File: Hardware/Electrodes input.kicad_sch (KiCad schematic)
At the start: 36 parts, among them J2 Conn_01x26_Pin, U10 TPD4E1B06DCKR, U2 TPD4E1B06DCKR, U3 TPD4E1B06DCKR, U4 TPD4E1B06DCKR, U5 TPD4E1B06DCKR, U9 TPD4E1B06DCKR

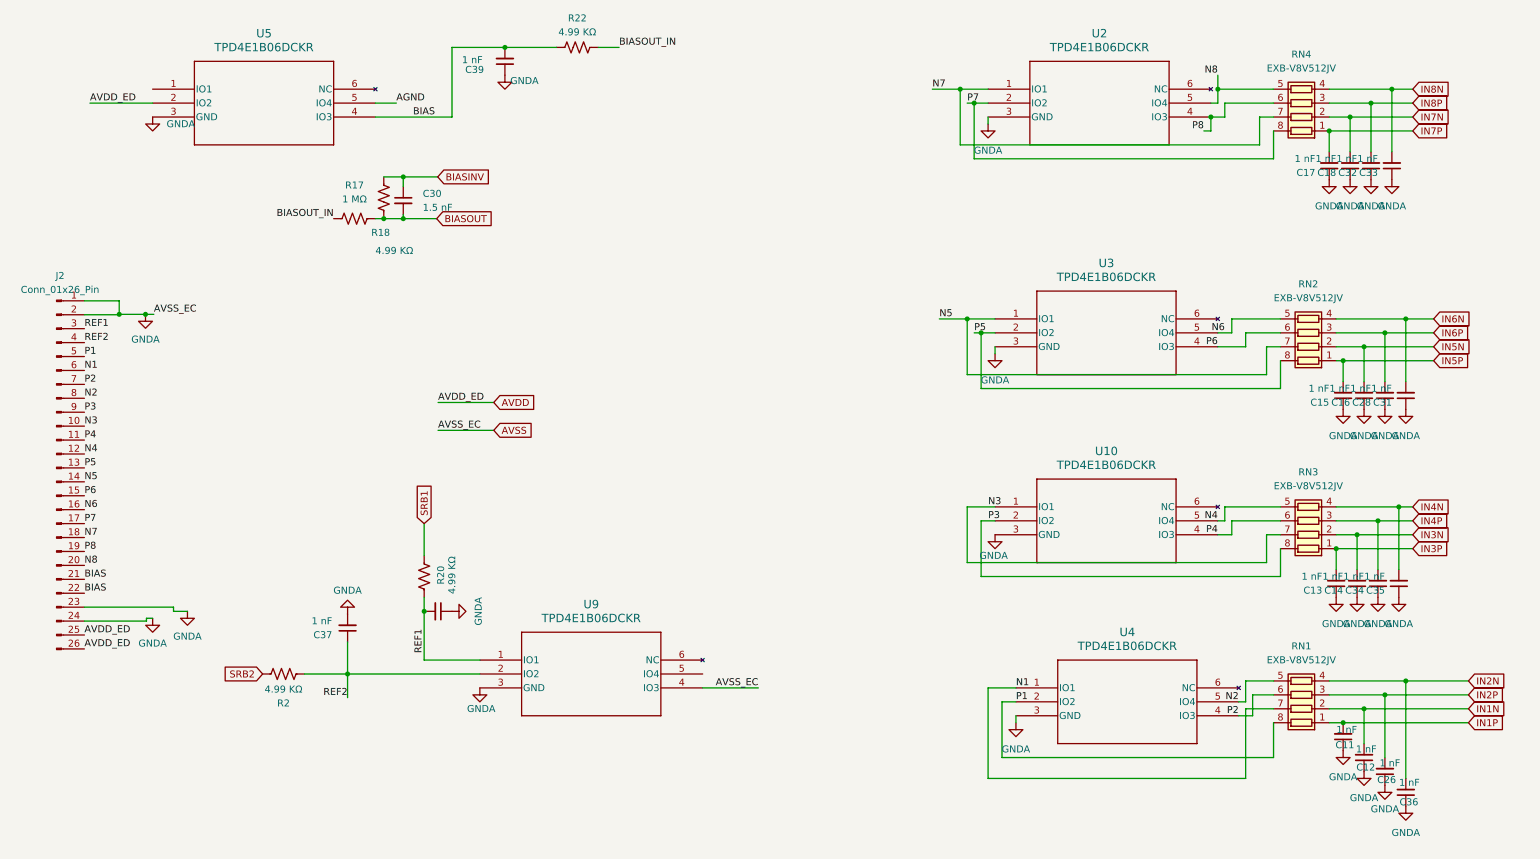
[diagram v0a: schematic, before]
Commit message: Fix GndA Avss connection, standardize grids
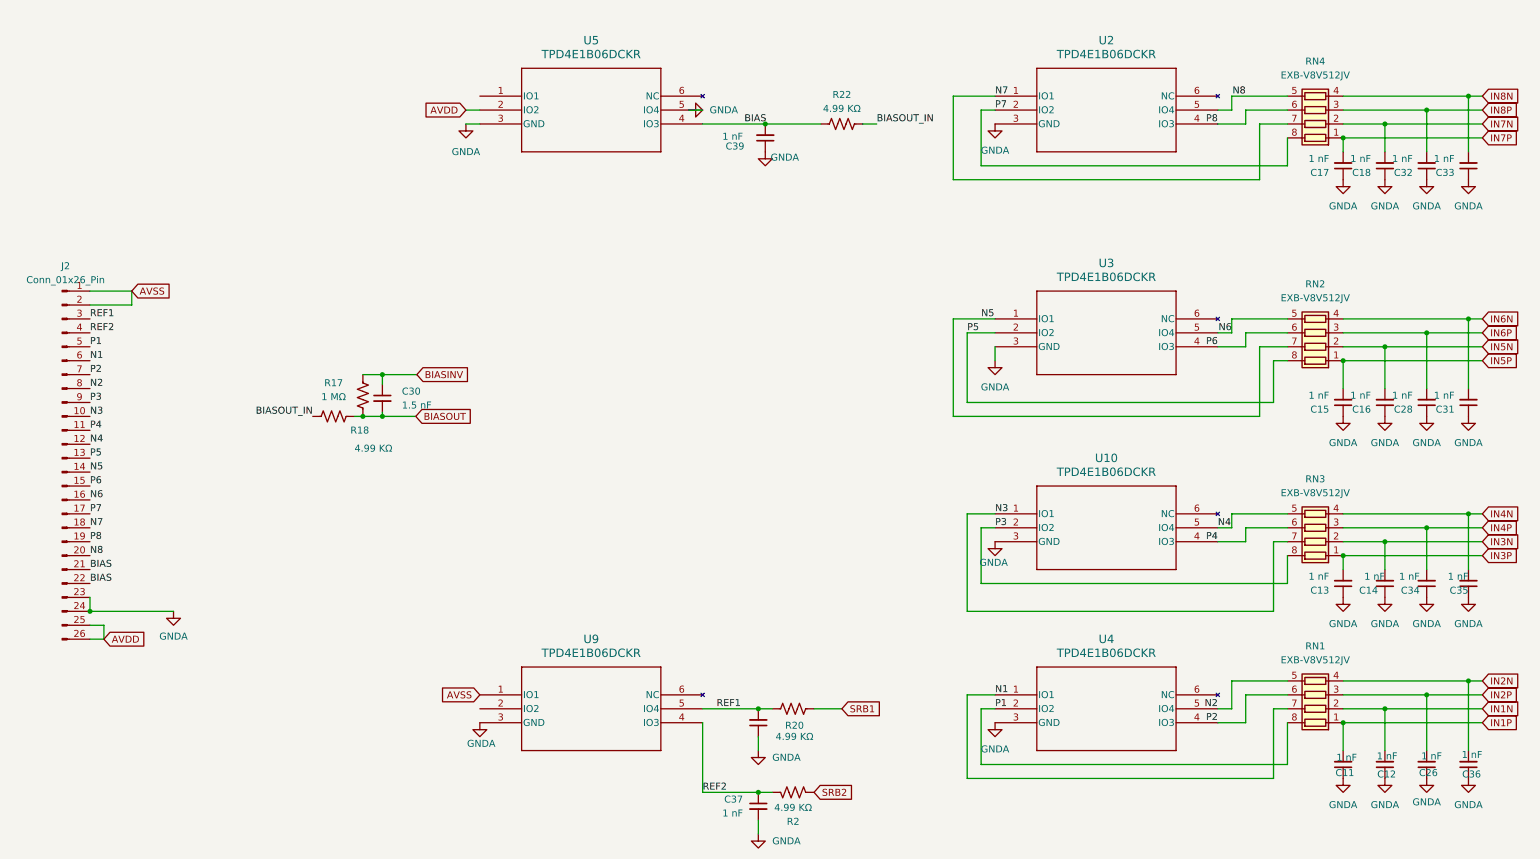
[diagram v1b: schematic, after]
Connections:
- net AGND is gone; now on net GNDA: U5.5 (IO4)
- net GNDA: no longer J2.1 (Pin_1), J2.2 (Pin_2), U9.4 (IO3)
- net REF1: now also U9.5 (IO4); no longer U9.1 (IO1)
- net REF2: now also U9.4 (IO3); no longer U9.2 (IO2)
- new net AVSS: J2.1 (Pin_1), J2.2 (Pin_2), U9.1 (IO1)
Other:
- moved on the sheet: C11, C12, C13, C14, C15, C16, C17, C18, C26, C28, C30, C31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
